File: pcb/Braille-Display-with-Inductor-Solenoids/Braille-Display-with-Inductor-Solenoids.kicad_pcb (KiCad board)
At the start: 2 copper layers, 58.2 x 57.4 mm, 58 parts, among them J1 Screw_Terminal_01x02, J2 Screw_Terminal_01x02, J3 Screw_Terminal_01x02, SW1 SW_Push, SW2 SW_Push, U1 RP2040-Zero, U2 TPIC6595, U3 TPIC6595, U4 TPIC6595

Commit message: Finish up board
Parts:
- added D1: LED, LED_SMD:LED_1206_3216Metric_Pad1.42x1.75mm_HandSolder, F.Cu at (121.5, 140.5)
- added R22: 5k1, Resistor_SMD:R_1206_3216Metric_Pad1.30x1.75mm_HandSolder, F.Cu at (121.5, 144.4)
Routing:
- net GND: track 0.00 -> 189.5 mm, vias 0 -> 40
- net VDC: track 0.00 -> 109.0 mm, vias 0 -> 4
- net /SHIFT_SER_IN: track 0.00 -> 73.3 mm
- net /SHIFT_SRCK: track 0.00 -> 69.7 mm
- net /SHIFT_RCLK: track 0.00 -> 66.7 mm, vias 0 -> 1
- net /SHIFT_G: track 0.00 -> 66.4 mm
- net Net-(L14-Pad2): track 0.00 -> 66.3 mm
- net Net-(L13-Pad2): track 0.00 -> 61.3 mm
- net +5V: track 0.00 -> 59.6 mm
- net /Braille_Cell2/DOT3_B: track 0.00 -> 42.0 mm, vias 0 -> 2
- net /Braille_Cell2/DOT3_A: track 0.00 -> 38.2 mm, vias 0 -> 2
- net Net-(L16-Pad2): track 0.00 -> 36.3 mm
- net /Braille_Cell2/DOT1_A: track 0.00 -> 35.6 mm, vias 0 -> 2
- net /Braille_Cell2/DOT2_A: track 0.00 -> 34.7 mm, vias 0 -> 2
- net /Braille_Cell1/SER_OUT: track 0.00 -> 33.9 mm, vias 0 -> 2
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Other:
- board text added: "3V3 GND"
- board text added: "GND 5V0"
- board text added: "Rev 1 2024-10-24 Vertical SMD Braille"
- board text added: "Select VDC Power"
- board text added: "VDC_LED"
- board text added: "V_IN GND"
- board text added: "V_IN or 5V"

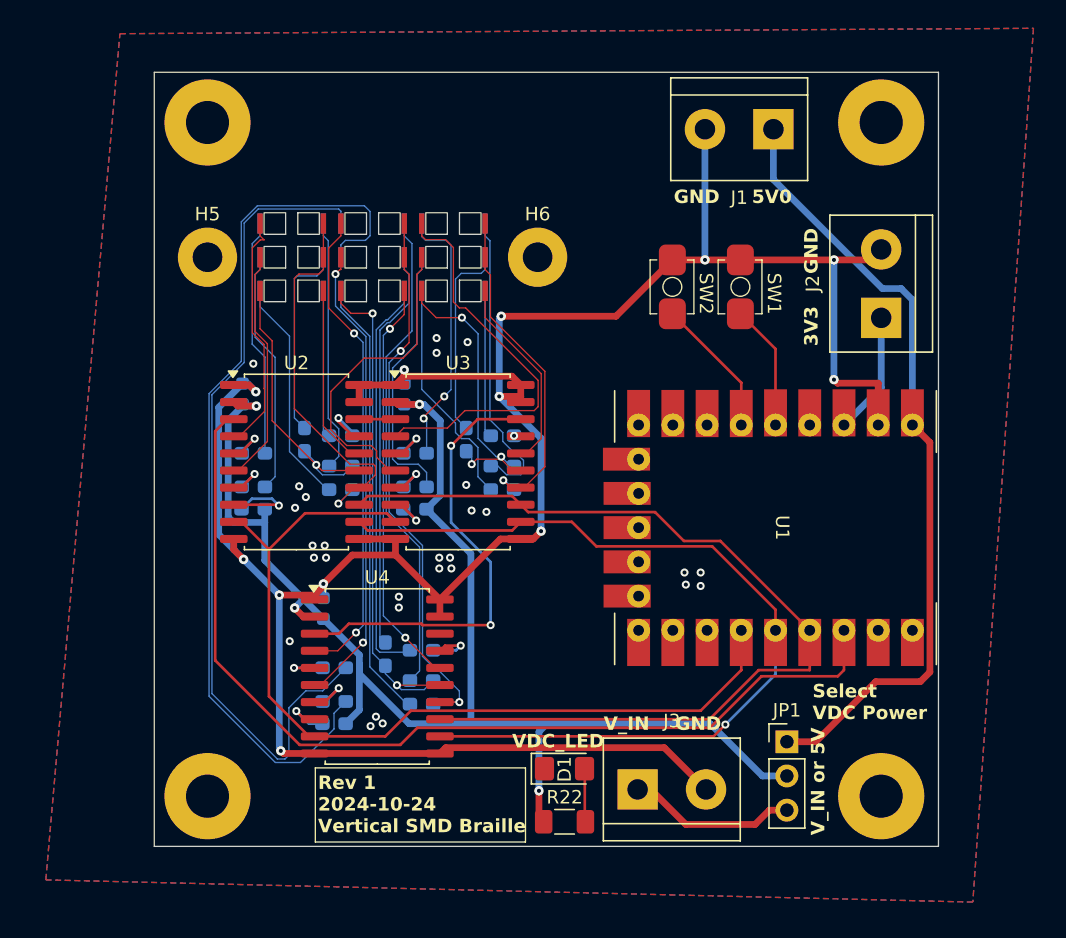
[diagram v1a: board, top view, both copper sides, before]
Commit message: Create flat inductor PCB
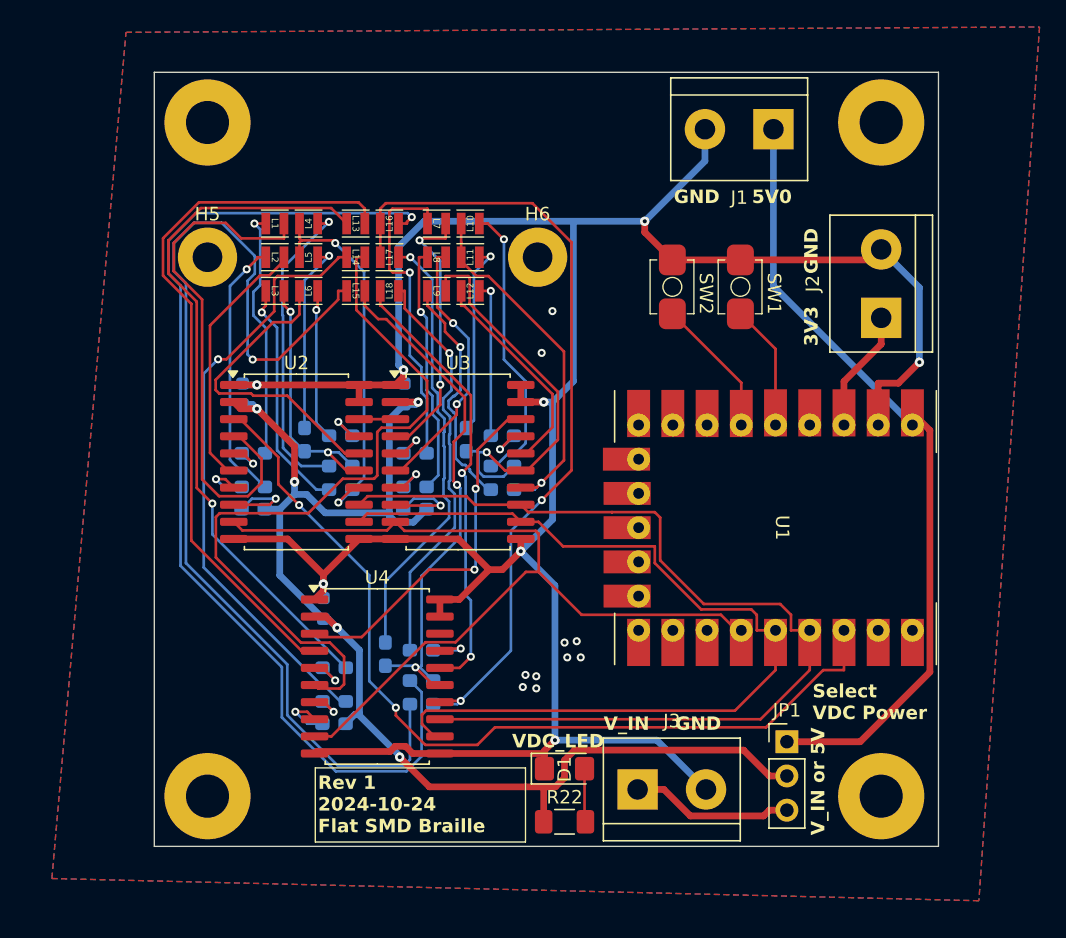
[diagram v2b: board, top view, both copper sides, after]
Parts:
- L1, L10, L11, L12, L13, L14, L15, L16, L17, L18, L2, L3, L4, L5, L6, L7, L8, L9: footprint 00-project-footprint-lib:Inductor_0805_2012Metric_SMD_Vertical_Square -> 00-project-footprint-lib:Inductor_VLS201612CX
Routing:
- net Net-(L15-Pad2): track 32.9 -> 78.7 mm, vias 0 -> 1
- net Net-(L16-Pad2): track 36.3 -> 77.6 mm, vias 0 -> 1
- net Net-(L14-Pad2): track 66.3 -> 44.7 mm, vias 0 -> 1
- net /Braille_Cell/DOT1_A: track 18.0 -> 38.6 mm
- net /Braille_Cell2/DOT2_A: track 34.7 -> 55.0 mm, vias 2 -> 0
- net /Braille_Cell2/DOT3_B: track 42.0 -> 60.3 mm
- net /Braille_Cell2/DOT1_A: track 35.6 -> 53.2 mm, vias 2 -> 0
- net VDC: track 109.0 -> 96.3 mm, vias 4 -> 5
- net GND: track 189.5 -> 202.1 mm, vias 40 -> 18
- net /Braille_Cell/DOT6_A: track 13.5 -> 23.3 mm
- net /Braille_Cell1/DOT1_A: track 29.8 -> 20.2 mm, vias 0 -> 2
- net Net-(L13-Pad2): track 61.3 -> 51.9 mm, vias 0 -> 1
- net /Braille_Cell1/DOT3_A: track 22.8 -> 30.6 mm, vias 3 -> 1
- net /Braille_Cell1/SER_OUT: track 33.9 -> 27.2 mm
- net /SHIFT_SER_IN: track 73.3 -> 66.7 mm, vias 0 -> 2
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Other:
- board text added: "2.5mm Intra-Cell Pitch. 6mm Inter-Cell Pitch X."
- board text added: "Rev 1 2024-10-24 Flat SMD Braille"
- board text removed: "2.5mm Intra-Cell Pitch. 6mm Inter-Cell Pitch X. For 0805 (2012 Metric) vertical SMD, chip is 2mm long. Use 1.6mm PCB."
- board text removed: "Rev 1 2024-10-24 Vertical SMD Braille"
